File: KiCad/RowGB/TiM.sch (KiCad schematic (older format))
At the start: 32 parts, among them P101 PWR_NW, P102 DO_N1, P103 DO_N2, P104 DI_N1, P105 DI_N2, P106 PWR_NE, P107 PWR_W, P108 PWR_E, P109 DI_W2, P110 DO_E2, P111 DI_W1, P112 DO_E1, P113 PWR_SW, P114 DI_S1, P115 DI_S2, P116 DO_S1, P117 DO_S2, P118 PWR_SE, P119 CONN_1, P120 CONN_1, P121 CONN_1, P122 CONN_1, P123 CONN_1, P124 CONN_1, P125 G>H, P126 F>G, P127 E>F, P128 D>E, P129 C>D, P130 B>C, P131 A>B

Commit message: TiM : Booya !! Final checks required before prototype boards.
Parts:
- added L101: OSHW, OSHW_6mm, symbol CONN_1
- added L102: Wyolum, Logo-WL3, symbol CONN_1
- P101, P106, P108: footprint (none) -> SIL-PWR-2
- P102, P103, P110, P112, P116, P117: footprint (none) -> CONN_S
- P104, P105, P109, P111, P114, P115: footprint (none) -> CONN_N
- P107, P113, P118: footprint (none) -> SIL-PWR
- P119, P120, P121, P122, P123, P124: footprint (none) -> pad
- P125, P126, P127, P128, P129, P130, P131: footprint (none) -> ShortLink
- PCB101: footprint (none) -> PCB
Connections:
- no-connect marks 1 -> 3
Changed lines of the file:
@@
-EESchema Schematic File Version 2  date 2/13/2013 1:59:50 PM
+EESchema Schematic File Version 2  date 2/14/2013 6:27:22 PM
 LIBS:RowGB_sym
 LIBS:power
@@
 Sheet 1 9
 Title "TiM - The Intelligent Matrix"
-Date "13 feb 2013"
+Date "14 feb 2013"
 Rev ""
 Comp "WyoLum"
@@
 Comment4 ""
 $EndDescr
+NoConn ~ 3900 7500
+NoConn ~ 4150 7500
+$Comp
+L CONN_1 L101
+U 1 1 511CD9F8
+P 3900 7350
+F 0 "L101" H 3980 7350 40  0000 L CNN
+F 1 "OSHW" H 3900 7405 30  0001 C CNN
+F 2 "OSHW_6mm" H 3900 7505 30  0001 C CNN
+	1    3900 7350
+	0    -1   -1   0
+$EndComp
+$Comp
+L CONN_1 L102
+U 1 1 511CD9F5
+P 4150 7350
+F 0 "L102" H 4230 7350 40  0000 L CNN
+F 1 "Wyolum" H 4150 7405 30  0001 C CNN
+F 2 "Logo-WL3" H 4150 7505 30  0001 C CNN
+	1    4150 7350
+	0    -1   -1   0
+$EndComp
 NoConn ~ 4500 7500
 $Comp
@@
 F 0 "PCB101" H 4580 7350 40  0000 L CNN
 F 1 "CONN_1" H 4500 7405 30  0001 C CNN
+F 2 "PCB" H 4500 7505 30  0001 C CNN
 	1    4500 7350
 	0    -1   -1   0
@@
 F 0 "P123" H 2330 4000 40  0000 L CNN
 F 1 "CONN_1" H 2250 4055 30  0001 C CNN
+F 2 "pad" H 2250 4155 30  0001 C CNN
 	1    2250 4000
 	0    1    1    0
@@
 F 0 "P124" H 3730 4000 40  0000 L CNN
 F 1 "CONN_1" H 3650 4055 30  0001 C CNN
+F 2 "pad" H 3650 4155 30  0001 C CNN
 	1    3650 4000
 	0    1    1    0
@@
 F 0 "P122" H 5830 3100 40  0000 L CNN
 F 1 "CONN_1" H 5750 3155 30  0001 C CNN
+F 2 "pad" H 5750 3255 30  0001 C CNN
 	1    5750 3100
 	1    0    0    -1
@@
 F 0 "P120" H 3730 1350 40  0000 L CNN
 F 1 "CONN_1" H 3650 1405 30  0001 C CNN
+F 2 "pad" H 3650 1505 30  0001 C CNN
 	1    3650 1350
 	0    -1   -1   0
@@
 F 0 "P119" H 2330 1350 40  0000 L CNN
 F 1 "CONN_1" H 2250 1405 30  0001 C CNN
+F 2 "pad" H 2250 1505 30  0001 C CNN
 	1    2250 1350
 	0    -1   -1   0
@@
 F 0 "P121" H 1130 3100 40  0000 L CNN
 F 1 "CONN_1" H 1050 3155 30  0001 C CNN
+F 2 "pad" H 1050 3255 30  0001 C CNN
 	1    1050 3100
 	-1   0    0    1
@@
 F 0 "P125" V 6150 5700 50  0000 C CNN
 F 1 "G>H" V 6250 5700 50  0000 C CNN
+F 2 "ShortLink" V 6350 5700 50  0001 C CNN
 F 4 "CONN HEADER 50POS .100\" SGL GOLD" H 6200 5800 60  0001 L CNN "Field4"
 F 5 "Header, Unshrouded, Male pin," H 6200 5900 60  0001 L CNN "Field5"
@@
 F 0 "P126" V 6150 6000 50  0000 C CNN
 F 1 "F>G" V 6250 6000 50  0000 C CNN
+F 2 "ShortLink" V 6350 6000 50  0001 C CNN
 F 4 "CONN HEADER 50POS .100\" SGL GOLD" H 6200 6100 60  0001 L CNN "Field4"
 F 5 "Header, Unshrouded, Male pin," H 6200 6200 60  0001 L CNN "Field5"
@@
 F 0 "P127" V 6150 6300 50  0000 C CNN
 F 1 "E>F" V 6250 6300 50  0000 C CNN
+F 2 "ShortLink" V 6350 6300 50  0001 C CNN
 F 4 "CONN HEADER 50POS .100\" SGL GOLD" H 6200 6400 60  0001 L CNN "Field4"
 F 5 "Header, Unshrouded, Male pin," H 6200 6500 60  0001 L CNN "Field5"
@@
 F 0 "P128" V 6150 6600 50  0000 C CNN
 F 1 "D>E" V 6250 6600 50  0000 C CNN
+F 2 "ShortLink" V 6350 6600 50  0001 C CNN
 F 4 "CONN HEADER 50POS .100\" SGL GOLD" H 6200 6700 60  0001 L CNN "Field4"
 F 5 "Header, Unshrouded, Male pin," H 6200 6800 60  0001 L CNN "Field5"
@@
 F 0 "P129" V 6150 6900 50  0000 C CNN
 F 1 "C>D" V 6250 6900 50  0000 C CNN
+F 2 "ShortLink" V 6350 6900 50  0001 C CNN
 F 4 "CONN HEADER 50POS .100\" SGL GOLD" H 6200 7000 60  0001 L CNN "Field4"
 F 5 "Header, Unshrouded, Male pin," H 6200 7100 60  0001 L CNN "Field5"
@@
 F 0 "P130" V 6150 7200 50  0000 C CNN
 F 1 "B>C" V 6250 7200 50  0000 C CNN
+F 2 "ShortLink" V 6350 7200 50  0001 C CNN
 F 4 "CONN HEADER 50POS .100\" SGL GOLD" H 6200 7300 60  0001 L CNN "Field4"
 F 5 "Header, Unshrouded, Male pin," H 6200 7400 60  0001 L CNN "Field5"
@@
 F 0 "P131" V 6150 7500 50  0000 C CNN
 F 1 "A>B" V 6250 7500 50  0000 C CNN
+F 2 "ShortLink" V 6350 7500 50  0001 C CNN
 F 4 "CONN HEADER 50POS .100\" SGL GOLD" H 6200 7600 60  0001 L CNN "Field4"
 F 5 "Header, Unshrouded, Male pin," H 6200 7700 60  0001 L CNN "Field5"
@@
 F 0 "P117" V 4250 4200 50  0000 C CNN
 F 1 "DO_S2" V 4350 4200 50  0000 C CNN
+F 2 "CONN_S" V 4450 4200 50  0001 C CNN
 F 4 "CONN RCPT 4POS .100\" SNGL HORZ" H 4300 4300 60  0001 L CNN "Field4"
 F 5 "Header, Female" H 4300 4400 60  0001 L CNN "Field5"
@@
 F 0 "P116" V 3850 4200 50  0000 C CNN
 F 1 "DO_S1" V 3950 4200 50  0000 C CNN
+F 2 "CONN_S" V 4050 4200 50  0001 C CNN
 F 4 "CONN RCPT 4POS .100\" SNGL HORZ" H 3900 4300 60  0001 L CNN "Field4"
 F 5 "Header, Female" H 3900 4400 60  0001 L CNN "Field5"
@@
 F 0 "P115" V 2850 4200 50  0000 C CNN
 F 1 "DI_S2" V 2950 4200 50  0000 C CNN
+F 2 "CONN_N" V 3050 4200 50  0001 C CNN
 F 4 "CONN RCPT 4POS .100\" SNGL HORZ" H 2900 4300 60  0001 L CNN "Field4"
 F 5 "Header, Female" H 2900 4400 60  0001 L CNN "Field5"
@@
 F 0 "P114" V 2450 4200 50  0000 C CNN
 F 1 "DI_S1" V 2550 4200 50  0000 C CNN
+F 2 "CONN_N" V 2650 4200 50  0001 C CNN
 F 4 "CONN RCPT 4POS .100\" SNGL HORZ" H 2500 4300 60  0001 L CNN "Field4"
 F 5 "Header, Female" H 2500 4400 60  0001 L CNN "Field5"
@@
 F 0 "P110" V 5900 2450 50  0000 C CNN
 F 1 "DO_E2" V 6000 2450 50  0000 C CNN
+F 2 "CONN_S" V 6100 2450 50  0001 C CNN
 F 4 "CONN HEADER 50POS .100\" SGL GOLD" H 5950 2550 60  0001 L CNN "Field4"
 F 5 "Header, Unshrouded, Male pin," H 5950 2650 60  0001 L CNN "Field5"
@@
 F 0 "P112" V 5900 2850 50  0000 C CNN
 F 1 "DO_E1" V 6000 2850 50  0000 C CNN
+F 2 "CONN_S" V 6100 2850 50  0001 C CNN
 F 4 "CONN HEADER 50POS .100\" SGL GOLD" H 5950 2950 60  0001 L CNN "Field4"
 F 5 "Header, Unshrouded, Male pin," H 5950 3050 60  0001 L CNN "Field5"
@@
 F 0 "P109" V 800 2450 50  0000 C CNN
 F 1 "DI_W2" V 900 2450 50  0000 C CNN
+F 2 "CONN_N" V 1000 2450 50  0001 C CNN
 F 4 "CONN HEADER 50POS .100\" SGL GOLD" H 850 2550 60  0001 L CNN "Field4"
 F 5 "Header, Unshrouded, Male pin," H 850 2650 60  0001 L CNN "Field5"
@@
 F 0 "P111" V 800 2850 50  0000 C CNN
 F 1 "DI_W1" V 900 2850 50  0000 C CNN
+F 2 "CONN_N" V 1000 2850 50  0001 C CNN
 F 4 "CONN HEADER 50POS .100\" SGL GOLD" H 850 2950 60  0001 L CNN "Field4"
 F 5 "Header, Unshrouded, Male pin," H 850 3050 60  0001 L CNN "Field5"
@@
 F 0 "P105" V 4250 1150 50  0000 C CNN
 F 1 "DI_N2" V 4350 1150 50  0000 C CNN
+F 2 "CONN_N" V 4450 1150 50  0001 C CNN
 F 4 "CONN HEADER 16POS .100 R/A 30AU" H 4300 1250 60  0001 L CNN "Field4"
 F 5 "Header, Unshrouded, Male pin," H 4300 1350 60  0001 L CNN "Field5"
@@
 F 0 "P104" V 3850 1150 50  0000 C CNN
 F 1 "DI_N1" V 3950 1150 50  0000 C CNN
+F 2 "CONN_N" V 4050 1150 50  0001 C CNN
 F 4 "CONN HEADER 16POS .100 R/A 30AU" H 3900 1250 60  0001 L CNN "Field4"
 F 5 "Header, Unshrouded, Male pin," H 3900 1350 60  0001 L CNN "Field5"
@@
 F 0 "P103" V 2850 1150 50  0000 C CNN
 F 1 "DO_N2" V 2950 1150 50  0000 C CNN
+F 2 "CONN_S" V 3050 1150 50  0001 C CNN
 F 4 "CONN HEADER 16POS .100 R/A 30AU" H 2900 1250 60  0001 L CNN "Field4"
 F 5 "Header, Unshrouded, Male pin," H 2900 1350 60  0001 L CNN "Field5"
@@
 F 0 "P102" V 2450 1150 50  0000 C CNN
 F 1 "DO_N1" V 2550 1150 50  0000 C CNN
+F 2 "CONN_S" V 2650 1150 50  0001 C CNN
 F 4 "CONN HEADER 16POS .100 R/A 30AU" H 2500 1250 60  0001 L CNN "Field4"
 F 5 "Header, Unshrouded, Male pin," H 2500 1350 60  0001 L CNN "Field5"
@@
 F 0 "P108" V 5900 1750 50  0000 C CNN
 F 1 "PWR_E" V 6000 1750 50  0000 C CNN
+F 2 "SIL-PWR-2" V 6100 1750 50  0001 C CNN
 F 4 "CONN HEADER 50POS .100\" SGL GOLD" H 5950 1850 60  0001 L CNN "Field4"
 F 5 "Header, Unshrouded, Male pin," H 5950 1950 60  0001 L CNN "Field5"
@@
 F 0 "P107" V 800 1750 50  0000 C CNN
 F 1 "PWR_W" V 900 1750 50  0000 C CNN
+F 2 "SIL-PWR" V 1000 1750 50  0001 C CNN
 F 4 "CONN HEADER 50POS .100\" SGL GOLD" H 850 1850 60  0001 L CNN "Field4"
 F 5 "Header, Unshrouded, Male pin," H 850 1950 60  0001 L CNN "Field5"
@@
 F 0 "P106" V 4850 1150 50  0000 C CNN
 F 1 "PWR_NE" V 4950 1150 50  0000 C CNN
+F 2 "SIL-PWR-2" V 5050 1150 50  0001 C CNN
 F 4 "CONN HEADER 50POS .100\" SGL GOLD" H 4900 1250 60  0001 L CNN "Field4"
 F 5 "Header, Unshrouded, Male pin," H 4900 1350 60  0001 L CNN "Field5"
@@
 F 0 "P101" V 1850 1150 50  0000 C CNN
 F 1 "PWR_NW" V 1950 1150 50  0000 C CNN
+F 2 "SIL-PWR-2" V 2050 1150 50  0001 C CNN
 F 4 "CONN HEADER 50POS .100\" SGL GOLD" H 1900 1250 60  0001 L CNN "Field4"
 F 5 "Header, Unshrouded, Male pin," H 1900 1350 60  0001 L CNN "Field5"
@@
 F 0 "P118" V 4850 4200 50  0000 C CNN
 F 1 "PWR_SE" V 4950 4200 50  0000 C CNN
+F 2 "SIL-PWR" V 5050 4200 50  0001 C CNN
 F 4 "CONN HEADER 50POS .100\" SGL GOLD" H 4900 4300 60  0001 L CNN "Field4"
 F 5 "Header, Unshrouded, Male pin," H 4900 4400 60  0001 L CNN "Field5"
@@
 F 0 "P113" V 1850 4200 50  0000 C CNN
 F 1 "PWR_SW" V 1950 4200 50  0000 C CNN
+F 2 "SIL-PWR" V 2050 4200 50  0001 C CNN
 F 4 "CONN HEADER 50POS .100\" SGL GOLD" H 1900 4300 60  0001 L CNN "Field4"
 F 5 "Header, Unshrouded, Male pin," H 1900 4400 60  0001 L CNN "Field5"

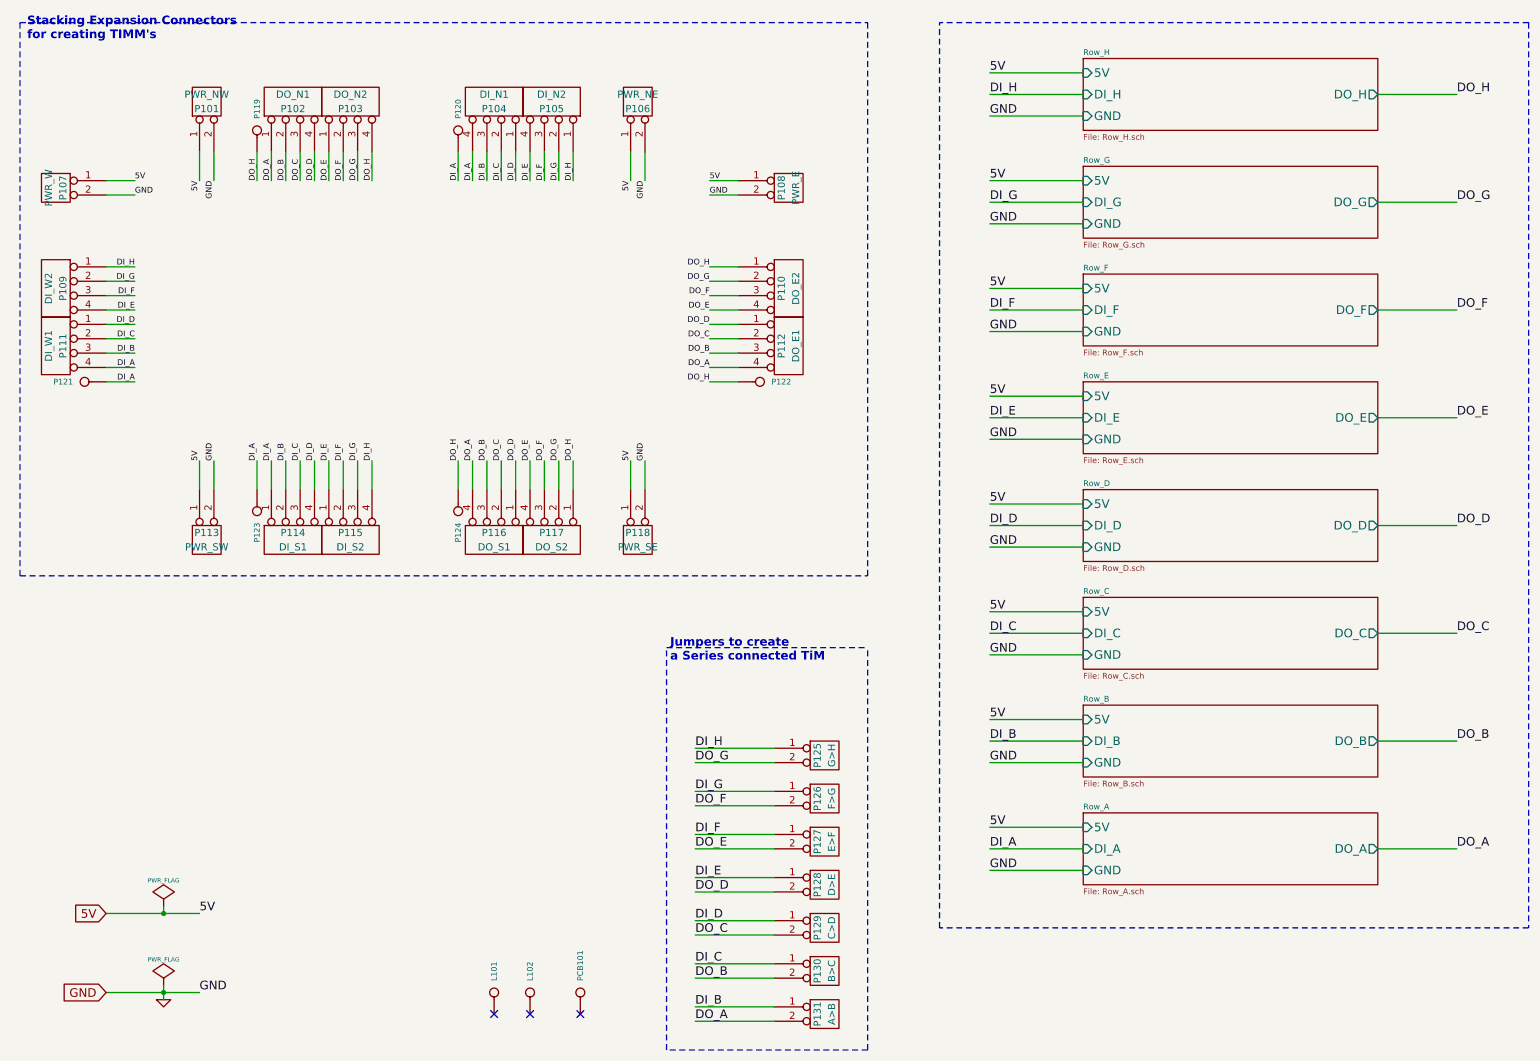
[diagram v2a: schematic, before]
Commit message: TIM : Legend clean up, added 2pin headers for Serial connections (easier to install). 3D update.
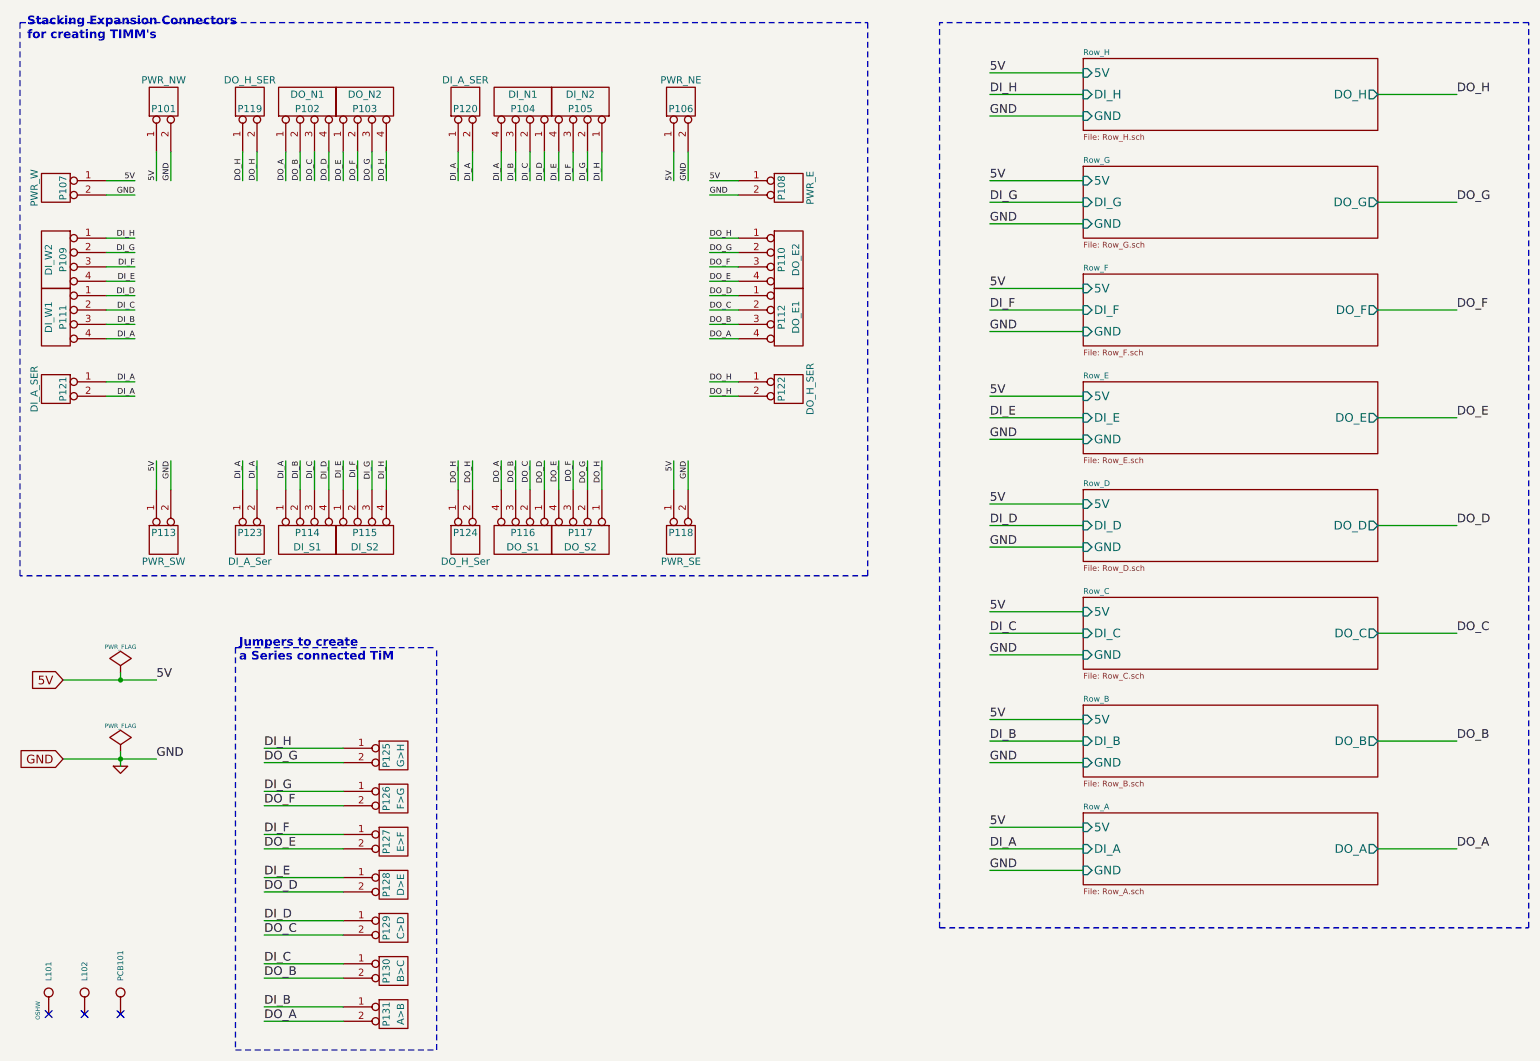
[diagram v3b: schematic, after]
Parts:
- removed P119, P120, P121, P122, P123, P124: CONN_1, pad, symbol CONN_1
- added P119, P122: DO_H_SER, SIL-PWR-2, symbol CONN_2
- added P120: DI_A_SER, SIL-PWR-2, symbol CONN_2
- added P121: DI_A_SER, SIL-PWR, symbol CONN_2
- added P123: DI_A_Ser, SIL-PWR, symbol CONN_2
- added P124: DO_H_Ser, SIL-PWR, symbol CONN_2
- P125, P126, P127, P128, P129, P130, P131: footprint ShortLink -> ShortLink2
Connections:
- net DI_A: now also P120.1 (P1), P120.2 (P2), P121.1 (P1), P121.2 (P2), P123.1 (P1), P123.2 (P2)
- net DO_H: now also P119.1 (P1), P119.2 (P2), P122.1 (P1), P122.2 (P2), P124.1 (P1), P124.2 (P2)
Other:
- moved on the sheet: L101, L102, P101, P102, P103, P104, P105, P106, P109, P110, P111, P112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
